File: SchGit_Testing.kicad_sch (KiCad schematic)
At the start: 3 parts

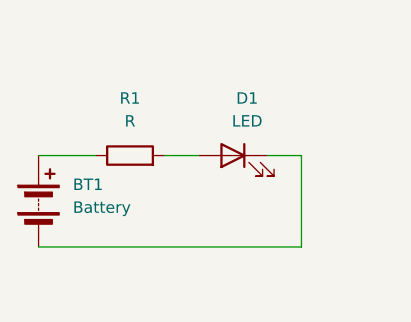
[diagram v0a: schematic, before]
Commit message: Added 2nd LED
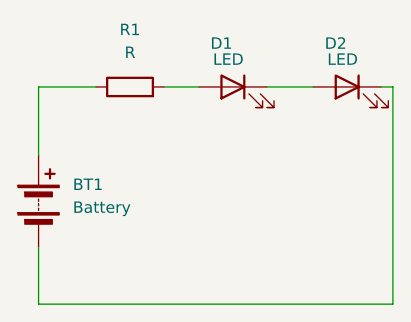
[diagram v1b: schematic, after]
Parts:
- added D2: LED, symbol Device:LED
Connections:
- net at BT1.2 (-): now also D2.1 (K); no longer D1.1 (K)
- new net: D1.1 (K), D2.2 (A)
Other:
- moved on the sheet: D1, R1
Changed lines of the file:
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@@
 	(wire
 		(pts
-			(xy 87.63 76.2) (xy 116.84 76.2)
-		)
-		(stroke
-			(width 0)
-			(type default)
-		)
-	)
-	(wire
-		(pts
-			(xy 116.84 66.04) (xy 113.03 66.04)
-		)
-		(stroke
-			(width 0)
-			(type default)
-		)
-	)
-	(wire
-		(pts
-			(xy 87.63 66.04) (xy 93.98 66.04)
-		)
-		(stroke
-			(width 0)
-			(type default)
-		)
-	)
-	(wire
-		(pts
-			(xy 116.84 76.2) (xy 116.84 66.04)
-		)
-		(stroke
-			(width 0)
-			(type default)
-		)
-	)
-	(wire
-		(pts
-			(xy 101.6 66.04) (xy 105.41 66.04)
+			(xy 87.63 82.55) (xy 87.63 76.2)
+		)
+		(stroke
+			(width 0)
+			(type default)
+		)
+	)
+	(wire
+		(pts
+			(xy 127 58.42) (xy 125.73 58.42)
+		)
+		(stroke
+			(width 0)
+			(type default)
+		)
+	)
+	(wire
+		(pts
+			(xy 87.63 58.42) (xy 87.63 66.04)
+		)
+		(stroke
+			(width 0)
+			(type default)
+		)
+	)
+	(wire
+		(pts
+			(xy 87.63 82.55) (xy 127 82.55)
+		)
+		(stroke
+			(width 0)
+			(type default)
+		)
+	)
+	(wire
+		(pts
+			(xy 87.63 58.42) (xy 93.98 58.42)
+		)
+		(stroke
+			(width 0)
+			(type default)
+		)
+	)
+	(wire
+		(pts
+			(xy 118.11 58.42) (xy 113.03 58.42)
+		)
+		(stroke
+			(width 0)
+			(type default)
+		)
+	)
+	(wire
+		(pts
+			(xy 127 82.55) (xy 127 58.42)
+		)
+		(stroke
+			(width 0)
+			(type default)
+		)
+	)
+	(wire
+		(pts
+			(xy 101.6 58.42) (xy 105.41 58.42)
 		)
 		(stroke
@@
 	(symbol
 		(lib_id "Device:LED")
-		(at 109.22 66.04 0)
+		(at 121.92 58.42 0)
 		(mirror y)
 		(unit 1)
@@
 		(in_pos_files yes)
 		(dnp no)
-		(fields_autoplaced yes)
+		(property "Reference" "D2"
+			(at 120.65 53.594 0)
+			(show_name no)
+			(do_not_autoplace no)
+			(effects
+				(font
+					(size 1.27 1.27)
+				)
+			)
+		)
+		(property "Value" "LED"
+			(at 121.412 55.372 0)
+			(show_name no)
+			(do_not_autoplace no)
+			(effects
+				(font
+					(size 1.27 1.27)
+				)
+			)
+		)
+		(property "Footprint" ""
+			(at 121.92 58.42 0)
+			(hide yes)
+			(show_name no)
+			(do_not_autoplace no)
+			(effects
+				(font
+					(size 1.27 1.27)
+				)
+			)
+		)
+		(property "Datasheet" ""
+			(at 121.92 58.42 0)
+			(hide yes)
+			(show_name no)
+			(do_not_autoplace no)
+			(effects
+				(font
+					(size 1.27 1.27)
+				)
+			)
+		)
+		(property "Description" "Light emitting diode"
+			(at 121.92 58.42 0)
+			(hide yes)
+			(show_name no)
+			(do_not_autoplace no)
+			(effects
+				(font
+					(size 1.27 1.27)
+				)
+			)
+		)
+		(property "Sim.Pins" "1=K 2=A"
+			(at 121.92 58.42 0)
+			(hide yes)
+			(show_name no)
+			(do_not_autoplace no)
+			(effects
+				(font
+					(size 1.27 1.27)
+				)
+			)
+		)
+		(pin "2"
+		)
+		(pin "1"
+		)
+		(instances
+			(project "SchGit_Testing"
+				(path "/c9fb6d08-8d28-4e50-9811-11520bd59fe8"
+					(reference "D2")
+					(unit 1)
+				)
+			)
+		)
+	)
+	(symbol
+		(lib_id "Device:LED")
+		(at 109.22 58.42 0)
+		(mirror y)
+		(unit 1)
+		(body_style 1)
+		(exclude_from_sim no)
+		(in_bom yes)
+		(on_board yes)
+		(in_pos_files yes)
+		(dnp no)
 		(property "Reference" "D1"
-			(at 110.8075 59.69 0)
+			(at 107.95 53.594 0)
 			(show_name no)
 			(do_not_autoplace no)
@@
 		)
 		(property "Value" "LED"
-			(at 110.8075 62.23 0)
+			(at 108.712 55.372 0)
 			(show_name no)
 			(do_not_autoplace no)
@@
 		)
 		(property "Footprint" ""
-			(at 109.22 66.04 0)
+			(at 109.22 58.42 0)
 			(hide yes)
 			(show_name no)
@@
 		)
 		(property "Datasheet" ""
-			(at 109.22 66.04 0)
+			(at 109.22 58.42 0)
 			(hide yes)
 			(show_name no)
@@
 		)
 		(property "Description" "Light emitting diode"
-			(at 109.22 66.04 0)
+			(at 109.22 58.42 0)
 			(hide yes)
 			(show_name no)
@@
 		)
 		(property "Sim.Pins" "1=K 2=A"
-			(at 109.22 66.04 0)
+			(at 109.22 58.42 0)
 			(hide yes)
 			(show_name no)
@@
 	(symbol
 		(lib_id "Device:R")
-		(at 97.79 66.04 90)
+		(at 97.79 58.42 90)
 		(unit 1)
 		(body_style 1)
@@
 		(fields_autoplaced yes)
 		(property "Reference" "R1"
-			(at 97.79 59.69 90)
+			(at 97.79 52.07 90)
 			(show_name no)
 			(do_not_autoplace no)
@@
 		)
 		(property "Value" "R"
-			(at 97.79 62.23 90)
+			(at 97.79 54.61 90)
 			(show_name no)
 			(do_not_autoplace no)
@@
 		)
 		(property "Footprint" ""
-			(at 97.79 67.818 90)
+			(at 97.79 60.198 90)
 			(hide yes)
 			(show_name no)
@@
 		)
 		(property "Datasheet" ""
-			(at 97.79 66.04 0)
+			(at 97.79 58.42 0)
 			(hide yes)
 			(show_name no)
@@
 		)
 		(property "Description" "Resistor"
-			(at 97.79 66.04 0)
-			(hide yes)
-			(show_name no)
+			(at 97.79 58.42 0)
+			(hide yes)
+			(show_name no)
